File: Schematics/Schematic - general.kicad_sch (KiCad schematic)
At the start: 41 parts, among them J1 Audio Input, J2 Audio Output, J3 +9V, SW1 SW_Push, SW2 SW_Push, SW3 SW_Push, SW4 SW_Push, SW5 Active / passive pickup switch, U1 MCP6002, U2 LM78L05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

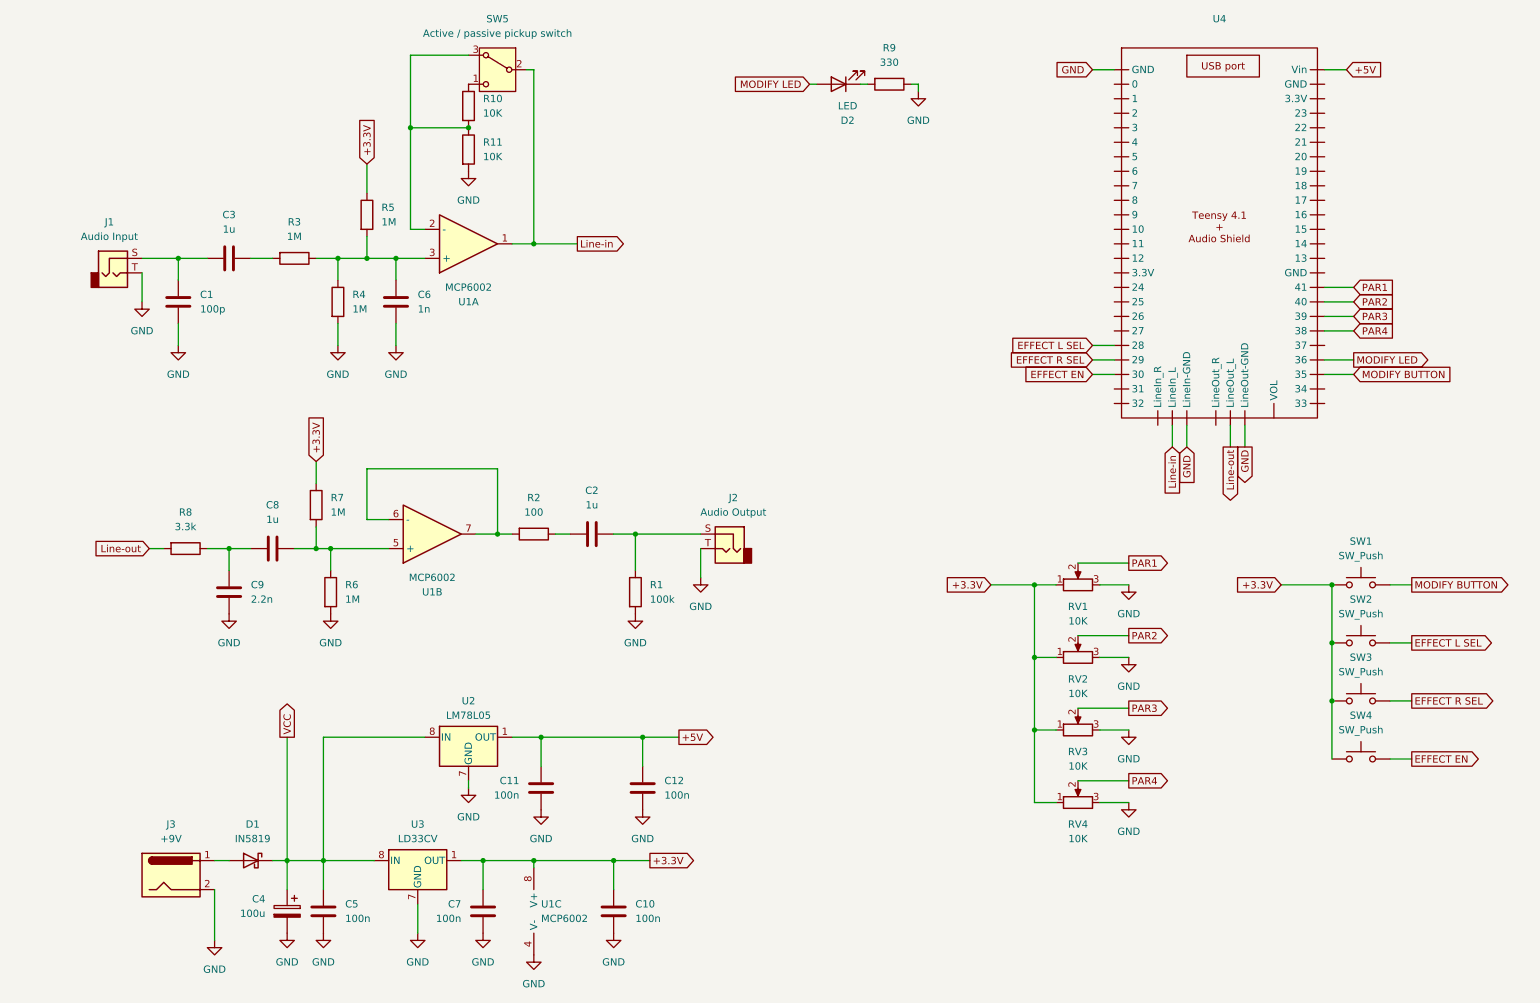
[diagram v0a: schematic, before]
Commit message: Started refactoring + pcb schematic work
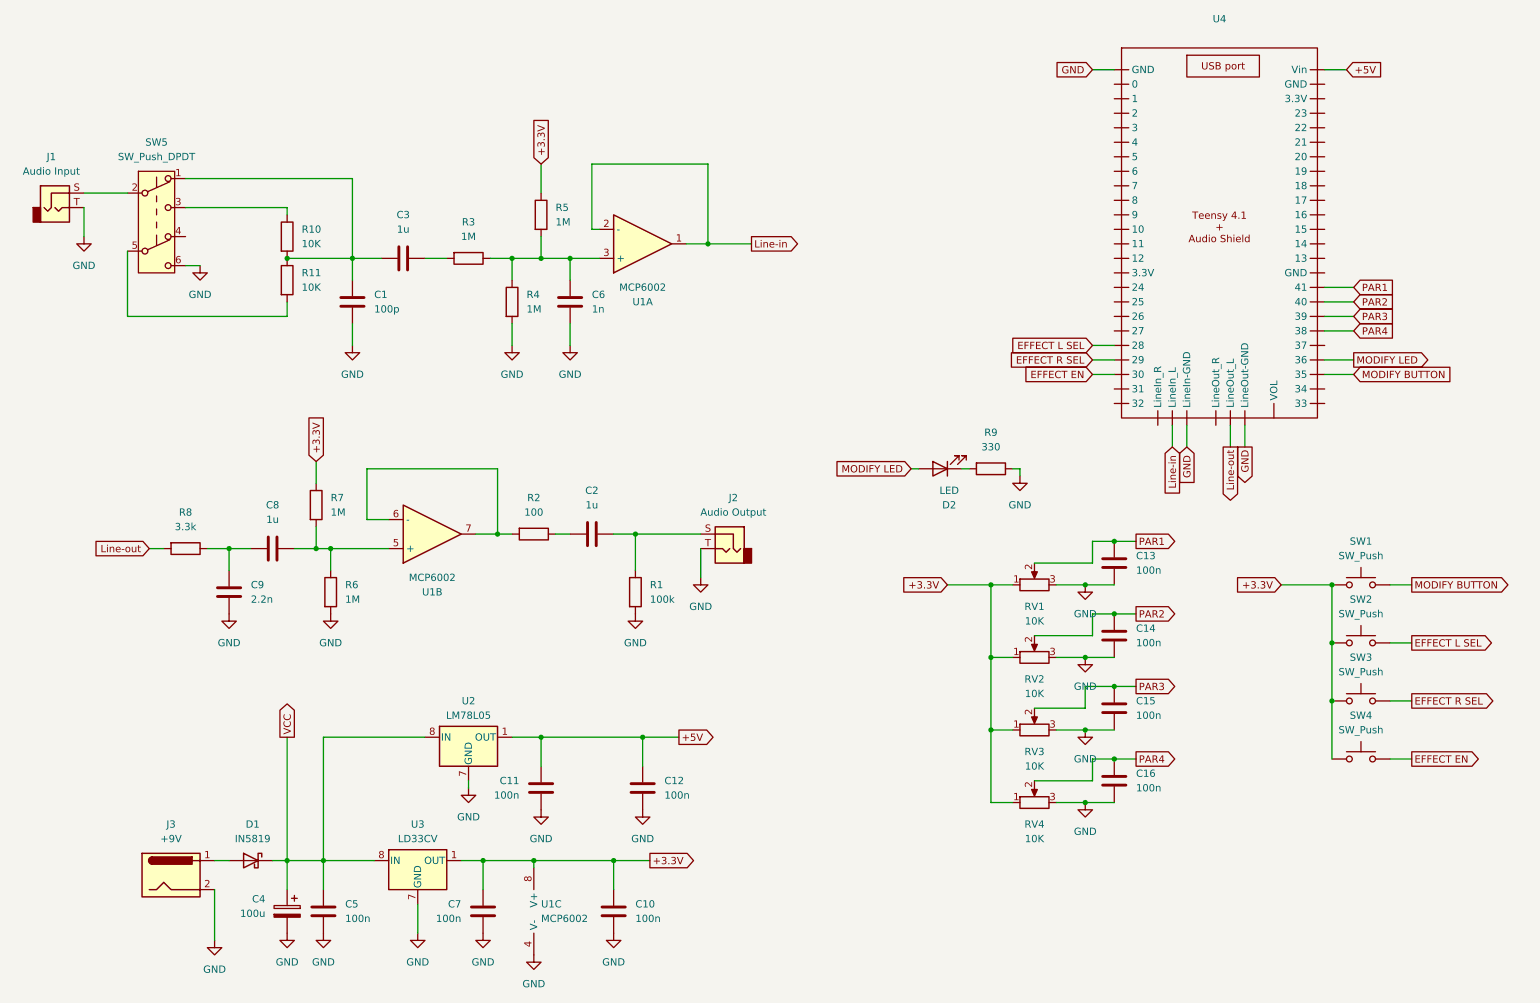
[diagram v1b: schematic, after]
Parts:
- removed SW5: Active / passive pickup switch, Button_Switch_SMD:Nidec_Copal_CAS-120A, symbol Switch:SW_Nidec_CAS-120A1
- added C13, C14, C15, C16: 100n, symbol Device:C
- added SW5: SW_Push_DPDT, symbol Switch:SW_Push_DPDT
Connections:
- net GND: now also C13.2, C14.2, C15.2, C16.2, SW5.6 (C); no longer R11.2
- net Line-in: now also U1.2 (-)
- net PAR1: now also C13.1
- net PAR2: now also C14.1
- net PAR3: now also C15.1
- net PAR4: now also C16.1
- net at R10.2, R11.1: now also C1.1, C3.2, SW5.1 (A); no longer U1.2 (-)
- net at R10.1: now also SW5.3 (C)
- new net: R11.2, SW5.5 (B)
- new net: J1.S, SW5.2 (B)
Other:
- moved on the sheet: C1, C3, C6, D2, J1, R10, R11, R3, R4, R5, R9, RV1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
